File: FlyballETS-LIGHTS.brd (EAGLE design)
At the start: 83.8 x 68.6 mm, 20 parts, among them IC1 74HC595N, IC2 ULN2003AN, IC3 LM555N

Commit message: Updated drawings and added PNG exports
- Added frames around drawings to make it look neater
- Added PNG export files so people who don't have EAGLE can see
everything
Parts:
- added U$1: (no value), frames:A4L-LOC
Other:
- board text added: "Alex Goris"
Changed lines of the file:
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@@
 http://bit.ly/1ErZ5QD
 LICENSE: CC-BY-SA</text>
+<text x="142.24" y="-48.26" size="2.54" layer="48">Alex Goris</text>
+<text x="88.9" y="-60.96" size="2.54" layer="48">FlyballETS
+LightsBoard v1
+http://bit.ly/1ErZ5QD
+LICENSE: CC-BY-SA</text>
+<dimension x1="83.82" y1="0" x2="83.82" y2="68.58" x3="93.98" y3="34.29" textsize="1.778" layer="48"/>
+<dimension x1="83.82" y1="68.58" x2="0" y2="68.58" x3="41.91" y3="78.74" textsize="1.778" layer="48"/>
 </plain>
 <attributes>
@@
 <element name="C2" library="resistor" package="C025-050X050" value="0.01uF" x="58.42" y="17.78" rot="R180"/>
 <element name="LSR" library="bt_con-jst-xh" package="B2B-XH" value="02-JST-B2B-XH-A" x="48.26" y="60.96"/>
+<element name="U$1" library="frames" package="A4L-LOC" value="" x="-76.2" y="-68.58"/>
 </elements>
 <signals>

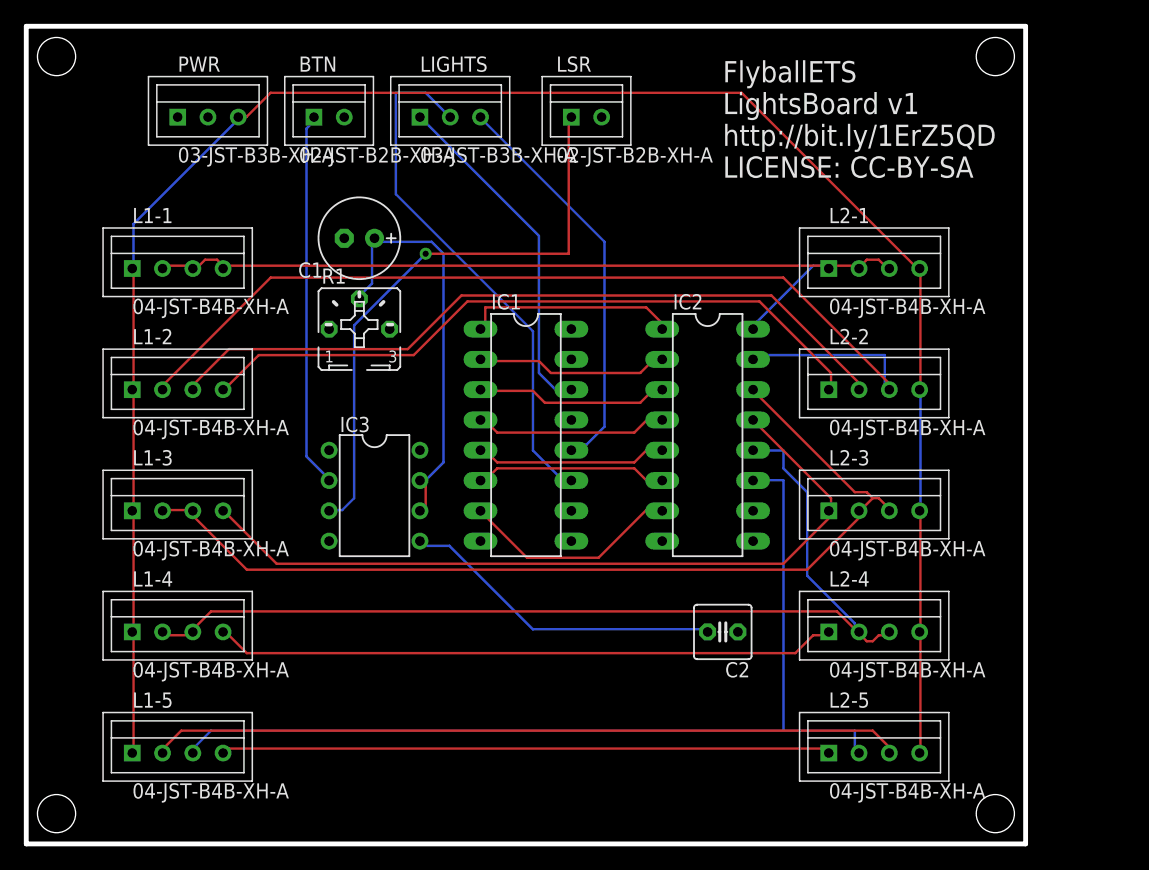
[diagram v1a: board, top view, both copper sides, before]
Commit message: v2 release of remaining boards.
- Lightsboard: Corrected swapped pin connections on L2 side and made
smaller
- Powerboard: Made smaller and added descriptions for LM2596 board
- Sensorboard: Made smaller
- All boards: Removed JST connector type names
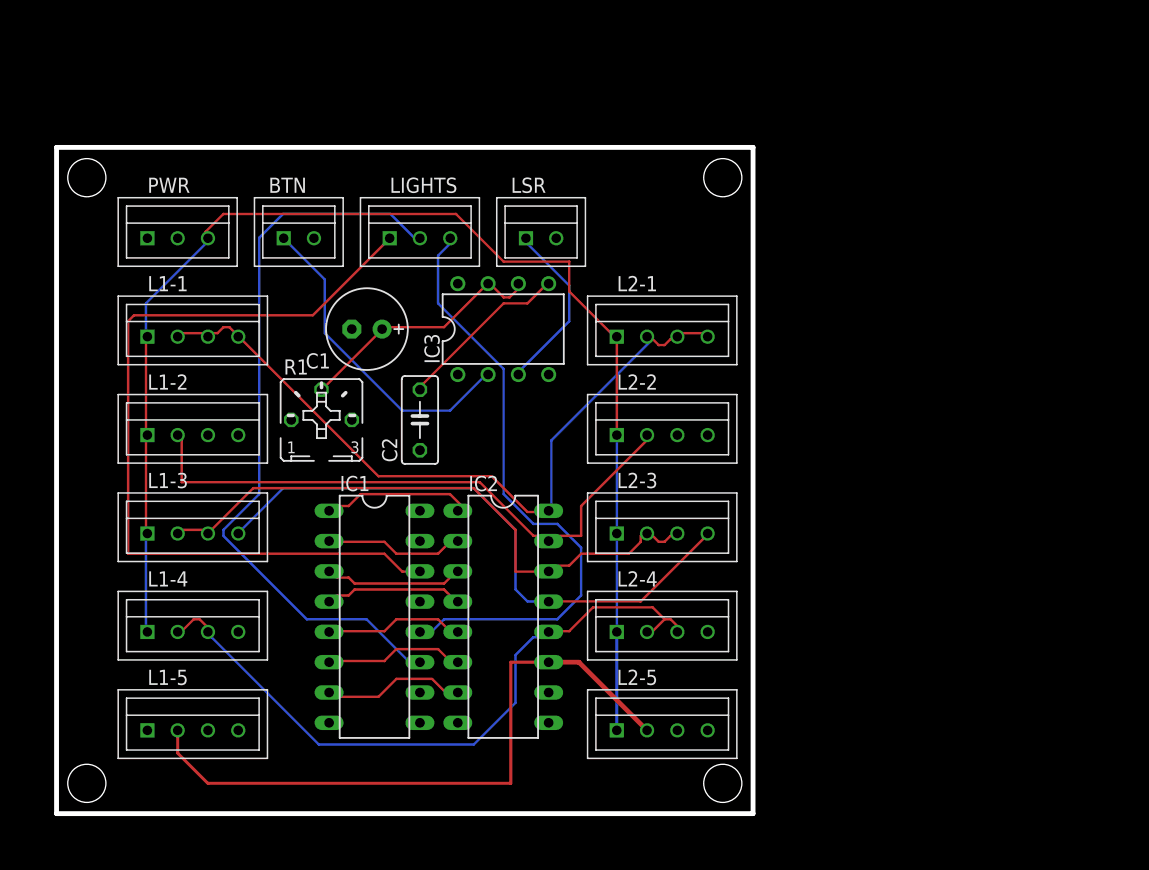
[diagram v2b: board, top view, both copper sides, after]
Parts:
- C2: value 0.01uF -> 10nF; device resistor:C025-050X050 -> resistor:C050-030X075
- moved C2 31.0 mm to (33.0, 35.6), turned to 90 degrees
- moved IC2 22.9 mm to (40.0, 19.1)
- moved IC1 19.8 mm to (29.2, 19.1)
- moved L2-1 18.7 mm to (53.3, 42.5)
- moved L2-2 18.2 mm to (53.3, 34.3)
- moved L2-3 17.9 mm to (53.3, 26.0)
- moved L2-5 17.9 mm to (53.3, 9.53)
- moved L2-4 17.8 mm to (53.3, 17.8)
- moved IC3 17.7 mm to (40.0, 43.2), turned to 0 degrees
- moved LSR 10.9 mm to (44.5, 50.8)
- moved BTN 10.5 mm to (24.1, 50.8)
- moved LIGHTS 10.5 mm to (33.0, 50.8)
- moved PWR 10.5 mm to (12.7, 50.8)
- moved R1 8.25 mm to (24.8, 35.6)
- moved C1 7.65 mm to (28.6, 43.2)
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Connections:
- removed net N$17: L1-2.P$3, L2-2.P$2
- removed net N$18: L1-2.P$4, L2-2.P$1
- removed net N$26: L1-4.P$4, L2-4.P$1
- removed net N$28: L1-5.P$2, L2-5.P$3
- removed net N$30: L1-5.P$4, L2-5.P$1
- net +12V: now also L2-1.P$1, L2-2.P$1, L2-3.P$1, L2-4.P$1, L2-5.P$1; no longer L2-1.P$4, L2-2.P$4, L2-3.P$4, L2-4.P$4, L2-5.P$4
- net N$13: now also L2-1.P$4; no longer L2-1.P$1
- net N$16: now also L2-2.P$2; no longer L2-2.P$3
- net N$22: now also L2-3.P$4; no longer L2-3.P$1
- net N$29: now also L1-5.P$2; no longer L1-5.P$3
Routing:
- net N$17: track 63.0 -> 0.00 mm
- net N$28: track 63.0 -> 0.00 mm
- net N$18: track 58.0 -> 0.00 mm
- net N$26: track 52.2 -> 0.00 mm
- net +12V: track 162.0 -> 109.9 mm
- net N$30: track 51.1 -> 0.00 mm
- net N$1: track 29.0 -> 69.4 mm
- net N$15: track 49.0 -> 14.6 mm, vias 1 -> 0
- net N$16: track 83.7 -> 50.7 mm
- net N$20: track 80.7 -> 51.1 mm
- net N$29: track 82.1 -> 54.9 mm
- net N$24: track 83.9 -> 58.0 mm
- net N$2: track 44.9 -> 62.6 mm
- net N$3: track 33.9 -> 51.3 mm
- net N$22: track 65.4 -> 50.2 mm
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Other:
- board size 83.8 x 68.6 mm -> 58.4 x 55.9 mm
- board text added: "FlyballETS LightsBoard v2 http://bit.ly/1ErZ5QD LICENSE: CC-BY-SA"
- board text removed: "FlyballETS LightsBoard v1 http://bit.ly/1ErZ5QD LICENSE: CC-BY-SA"

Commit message: LightsBoard:Fix 74HC595 problems
Closes #5
- Added decoupling capacitor over GND and VCC of 74HC595
- Added missing connection of 74HC595 pin10 to +5V
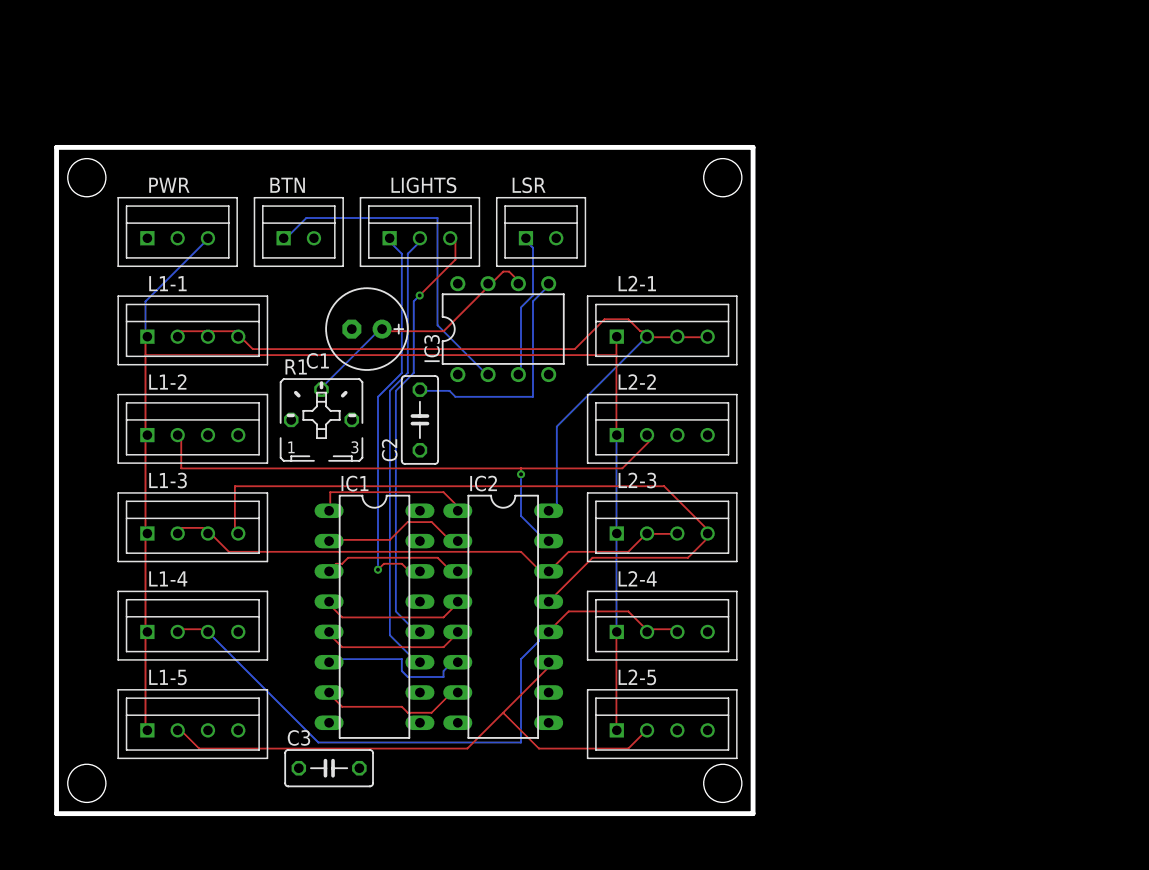
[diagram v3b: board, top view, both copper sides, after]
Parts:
- added C3: 100nF, resistor:C050-030X075
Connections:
- net +5V: now also C3.2, IC1.10
- net GND: now also C3.1
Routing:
- net N$1: track 69.4 -> 33.1 mm, vias 0 -> 1
- net N$2: track 62.6 -> 38.1 mm
- net N$3: track 51.3 -> 36.7 mm, vias 0 -> 1
- net N$22: track 50.2 -> 61.9 mm
- net +12V: track 109.9 -> 116.5 mm
- net N$20: track 51.1 -> 45.0 mm
- net N$29: track 54.9 -> 49.1 mm
- net N$12: track 14.6 -> 19.7 mm
- net N$13: track 62.6 -> 65.9 mm
- net N$15: track 14.6 -> 12.2 mm
- net N$24: track 58.0 -> 56.0 mm
- net N$9: track 11.7 -> 13.2 mm
- net N$14: track 27.0 -> 28.5 mm
- net N$4: track 12.8 -> 13.5 mm
- net N$16: track 50.7 -> 51.1 mm, vias 0 -> 1

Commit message: Fixed several issues
- Checked all mounting holes (fixes #1 )
- Marked light colors on lights PCB (fixes #7 )
- Swapped pins 2 and 3 on LIGHTS connected on PWR board (fixes #3 )
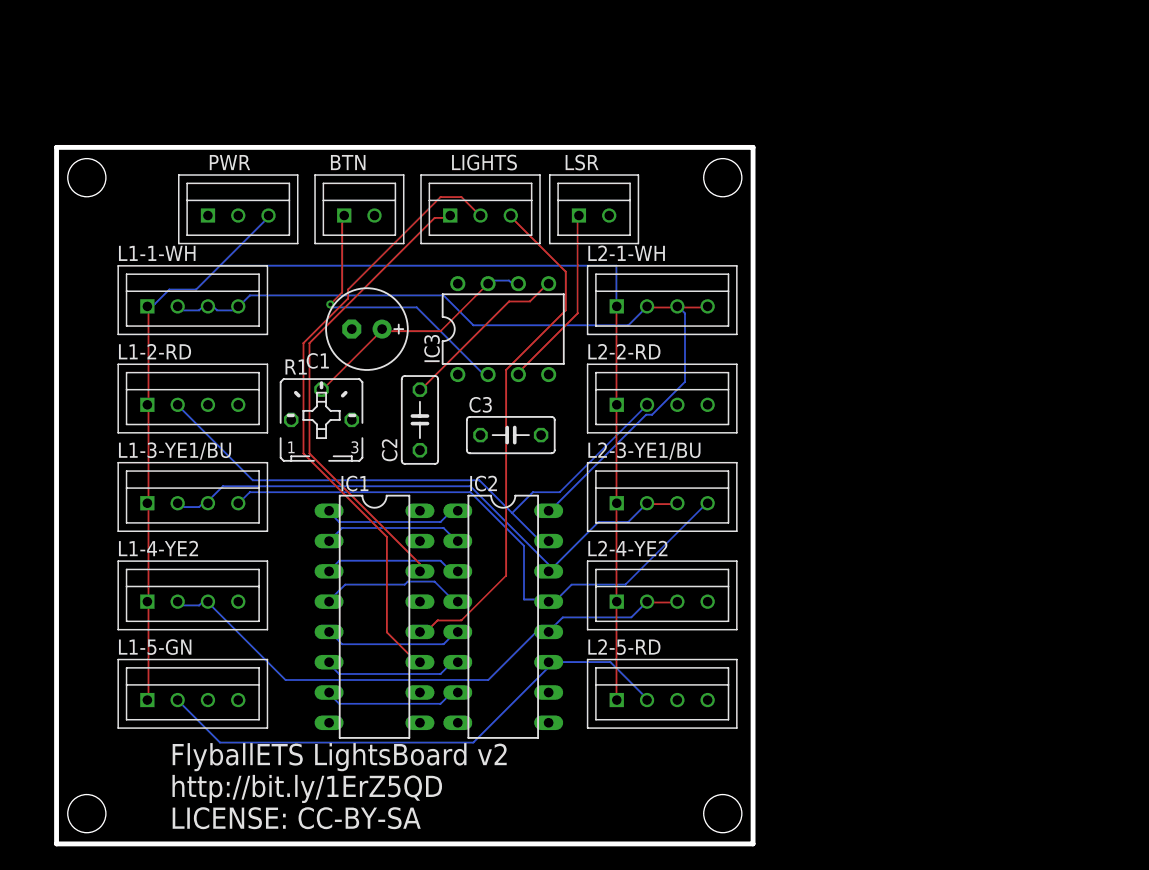
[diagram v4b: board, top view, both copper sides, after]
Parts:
- removed L1-1, L1-2, L1-3, L1-4, L1-5, L2-1, L2-2, L2-3, L2-4, L2-5: 04-JST-B4B-XH-A, bt_con-jst-xh:B4B-XH
- added L1-1-WH, L1-2-RD, L1-3-YE1/BU, L1-4-YE2, L1-5-GN, L2-1-WH, L2-2-RD, L2-3-YE1/BU, L2-4-YE2, L2-5-RD: 04-JST-B4B-XH-A, bt_con-jst-xh:B4B-XH
- moved C3 31.8 mm to (40.6, 34.3)
- moved BTN 5.43 mm to (29.2, 52.7)
- moved PWR 5.43 mm to (17.8, 52.7)
- moved LIGHTS 5.43 mm to (38.1, 52.7)
- moved LSR 4.84 mm to (48.9, 52.7)
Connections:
- net +12V: now also L1-1-WH.P$1, L1-2-RD.P$1, L1-3-YE1/BU.P$1, L1-4-YE2.P$1, L1-5-GN.P$1, L2-1-WH.P$1, L2-2-RD.P$1, L2-3-YE1/BU.P$1, L2-4-YE2.P$1, L2-5-RD.P$1; no longer L1-1.P$1, L1-2.P$1, L1-3.P$1, L1-4.P$1, L1-5.P$1, L2-1.P$1, L2-2.P$1, L2-3.P$1, L2-4.P$1, L2-5.P$1
- net N$13: now also L1-1-WH.P$2, L1-1-WH.P$3, L1-1-WH.P$4, L2-1-WH.P$2, L2-1-WH.P$3, L2-1-WH.P$4; no longer L1-1.P$2, L1-1.P$3, L1-1.P$4, L2-1.P$2, L2-1.P$3, L2-1.P$4
- net N$16: now also L1-2-RD.P$2, L2-2-RD.P$2; no longer L1-2.P$2, L2-2.P$2
- net N$20: now also L1-3-YE1/BU.P$2, L1-3-YE1/BU.P$3, L2-3-YE1/BU.P$2, L2-3-YE1/BU.P$3; no longer L1-3.P$2, L1-3.P$3, L2-3.P$2, L2-3.P$3
- net N$22: now also L1-3-YE1/BU.P$4, L2-3-YE1/BU.P$4; no longer L1-3.P$4, L2-3.P$4
- net N$24: now also L1-4-YE2.P$2, L1-4-YE2.P$3, L2-4-YE2.P$2, L2-4-YE2.P$3; no longer L1-4.P$2, L1-4.P$3, L2-4.P$2, L2-4.P$3
- net N$29: now also L1-5-GN.P$2, L2-5-RD.P$2; no longer L1-5.P$2, L2-5.P$2
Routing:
- net N$2: track 38.1 -> 52.3 mm
- net N$22: track 61.9 -> 49.6 mm
- net N$24: track 56.0 -> 47.7 mm
- net N$3: track 36.7 -> 43.3 mm, vias 1 -> 0
- net N$1: track 33.1 -> 39.3 mm, vias 1 -> 0
- net N$12: track 19.7 -> 14.5 mm
- net N$14: track 28.5 -> 23.6 mm, vias 0 -> 1
- net N$20: track 45.0 -> 49.1 mm
- net N$13: track 65.9 -> 69.7 mm
- net N$29: track 49.1 -> 45.4 mm
- net N$15: track 12.2 -> 15.4 mm
- net N$4: track 13.5 -> 11.6 mm
- net N$9: track 13.2 -> 11.7 mm
- net N$11: track 21.8 -> 20.6 mm
- net N$10: track 12.2 -> 11.6 mm
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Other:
- board size 58.4 x 55.9 mm -> 58.4 x 58.4 mm

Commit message: Fixed JST XH pin numbering
Updated bt_con-jst-xh.lbr library with swapped pin numbering.
Updated all board designs with updated library so they have the
connectors the right way around
Fixes #4
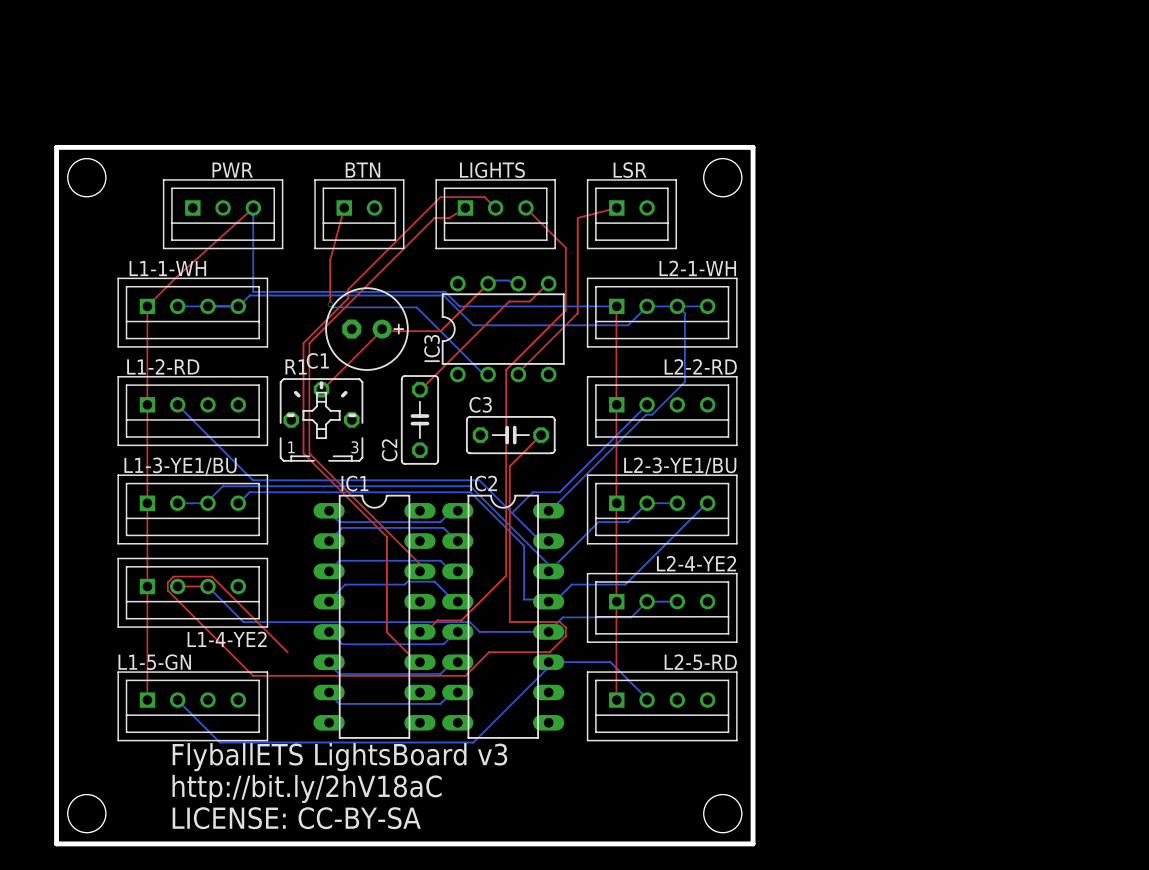
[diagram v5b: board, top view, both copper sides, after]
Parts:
- BTN, LSR: value 02-JST-B2B-XH-A -> 02-JST
- moved LSR 3.24 mm to (52.1, 53.3), turned to 180 degrees
- moved PWR 1.42 mm to (16.5, 53.3), turned to 180 degrees
- moved LIGHTS 1.42 mm to (39.4, 53.3), turned to 180 degrees
- moved L1-4-YE2 1.27 mm to (14.0, 21.6), turned to 180 degrees
- moved BTN 0.64 mm to (29.2, 53.3), turned to 180 degrees
- turned L1-1-WH to 180 degrees
- turned L1-2-RD to 180 degrees
- turned L1-3-YE1/BU to 180 degrees
- turned L1-5-GN to 180 degrees
- turned L2-1-WH to 180 degrees
- turned L2-2-RD to 180 degrees
- turned L2-3-YE1/BU to 180 degrees
- turned L2-4-YE2 to 180 degrees
- turned L2-5-RD to 180 degrees
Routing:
- net +5V: track 0.00 -> 73.7 mm
- net N$15: track 15.4 -> 18.6 mm
- net N$24: track 47.7 -> 44.6 mm
- net N$13: track 69.7 -> 71.6 mm
- net N$1: track 39.3 -> 40.6 mm
- net N$2: track 52.3 -> 53.3 mm
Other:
- board text added: "FlyballETS LightsBoard v3 http://bit.ly/2hV18aC LICENSE: CC-BY-SA"
- board text removed: "FlyballETS LightsBoard v2 http://bit.ly/1ErZ5QD LICENSE: CC-BY-SA"
